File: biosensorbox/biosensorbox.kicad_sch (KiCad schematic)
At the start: 42 parts, among them J1 USB_B_Mini, J2 ECG1, J3 ECG2, Q1 NMOS, SW1 BootButton, SW2 ResetButton, U1 ESP32-S3-WROOM-1, U2 TPD2EUSB30, U3 BMI270, U4 OPA325, U5 PUS-0503.3-2W

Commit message: Updated DC/DC Converter Capacitor values
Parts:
- C11: value 10u -> 0.47u
- C12: value 10u -> 33u
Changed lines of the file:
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@@
       (effects (font (size 1.27 1.27)) (justify left))
     )
-    (property "Value" "10u" (at 237.49 85.09 0)
+    (property "Value" "33u" (at 237.49 85.09 0)
       (effects (font (size 1.27 1.27)) (justify left))
     )
@@
       (effects (font (size 1.27 1.27)) (justify left))
     )
-    (property "Value" "10u" (at 273.05 85.09 0)
-      (effects (font (size 1.27 1.27)) (justify left))
-    )
+    (property "Value" "0.47u" (at 273.05 85.09 0)
+      (effects (font (size 1.27 1.27)) (justify left))
+    )

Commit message: Latest updates to the schematic
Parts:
- removed J2: ECG1, symbol Connector_Generic:Conn_01x01
- removed J3: ECG2, symbol Connector_Generic:Conn_01x01
- added J4: Display, symbol Connector_Generic:Conn_01x05
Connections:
- net GND: now also Q1.3 (S); no longer Q1.1 (D)
- net at R4.1, R5.1, R6.1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: now also Q1.1 (D); no longer Q1.3 (S)
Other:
- note removed: "TODO : ECG Electrodes + Instrumenting amplifier"
- moved on the sheet: Q1
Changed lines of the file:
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@@
-    (effects (font (size 1.27 1.27)) (justify left bottom))
-  )
-  (text "TODO : ECG Electrodes + Instrumenting amplifier" (at 106.68 151.13 0)
     (effects (font (size 1.27 1.27)) (justify left bottom))
   )
@@
     )
   )
-  (symbol (lib_id "Connector_Generic:Conn_01x01") (at 113.03 140.97 180) (unit 1)
-    (in_bom yes) (on_board yes) (dnp no) (fields_autoplaced)
-    (property "Reference" "J3" (at 113.03 134.62 0)
-      (effects (font (size 1.27 1.27)))
-    )
-    (property "Value" "ECG2" (at 113.03 137.16 0)
-      (effects (font (size 1.27 1.27)))
-    )
-    (property "Footprint" "" (at 113.03 140.97 0)
-      (effects (font (size 1.27 1.27)) hide)
-    )
-    (property "Datasheet" "~" (at 113.03 140.97 0)
-      (effects (font (size 1.27 1.27)) hide)
-    )
-    (pin "1")
-    (instances
-      (project "biosensorbox"
-        (path "/b5418477-9d8b-43d2-97f7-47051a4a367a"
-          (reference "J3") (unit 1)
-        )
-      )
-    )
-  )
   (symbol (lib_id "Device:R") (at 45.72 182.88 270) (mirror x) (unit 1)
     (in_bom yes) (on_board yes) (dnp no) (fields_autoplaced)
@@
         (path "/b5418477-9d8b-43d2-97f7-47051a4a367a"
           (reference "C10") (unit 1)
+        )
+      )
+    )
+  )
+  (symbol (lib_id "Connector_Generic:Conn_01x05") (at 185.42 140.97 270) (unit 1)
+    (in_bom yes) (on_board yes) (dnp no) (fields_autoplaced)
+    (property "Reference" "J4" (at 185.42 144.78 90)
+      (effects (font (size 1.27 1.27)))
+    )
+    (property "Value" "Display" (at 185.42 147.32 90)
+      (effects (font (size 1.27 1.27)))
+    )
+    (property "Footprint" "" (at 185.42 140.97 0)
+      (effects (font (size 1.27 1.27)) hide)
+    )
+    (property "Datasheet" "~" (at 185.42 140.97 0)
+      (effects (font (size 1.27 1.27)) hide)
+    )
+    (pin "2")
+    (pin "1")
+    (pin "3")
+    (pin "4")
+    (pin "5")
+    (instances
+      (project "biosensorbox"
+        (path "/b5418477-9d8b-43d2-97f7-47051a4a367a"
+          (reference "J4") (unit 1)
         )
       )
@@
     )
   )
-  (symbol (lib_id "Connector_Generic:Conn_01x01") (at 137.16 140.97 0) (unit 1)
-    (in_bom yes) (on_board yes) (dnp no)
-    (property "Reference" "J2" (at 135.89 134.62 0)
-      (effects (font (size 1.27 1.27)) (justify left))
-    )
-    (property "Value" "ECG1" (at 134.62 137.16 0)
-      (effects (font (size 1.27 1.27)) (justify left))
-    )
-    (property "Footprint" "" (at 137.16 140.97 0)
-      (effects (font (size 1.27 1.27)) hide)
-    )
-    (property "Datasheet" "~" (at 137.16 140.97 0)
-      (effects (font (size 1.27 1.27)) hide)
-    )
-    (pin "1")
-    (instances
-      (project "biosensorbox"
-        (path "/b5418477-9d8b-43d2-97f7-47051a4a367a"
-          (reference "J2") (unit 1)
-        )
-      )
-    )
-  )
   (symbol (lib_id "Device:Fuse") (at 274.32 78.74 90) (unit 1)
     (in_bom yes) (on_board yes) (dnp no) (fields_autoplaced)
@@
     )
   )
-  (symbol (lib_id "Simulation_SPICE:NMOS") (at 63.5 180.34 270) (unit 1)
-    (in_bom yes) (on_board yes) (dnp no) (fields_autoplaced)
+  (symbol (lib_id "Simulation_SPICE:NMOS") (at 63.5 180.34 90) (mirror x) (unit 1)
+    (in_bom yes) (on_board yes) (dnp no)
     (property "Reference" "Q1" (at 63.5 186.69 90)
       (effects (font (size 1.27 1.27)))
@@
       (effects (font (size 1.27 1.27)))
     )
-    (property "Footprint" "" (at 66.04 185.42 0)
-      (effects (font (size 1.27 1.27)) hide)
-    )
-    (property "Datasheet" "https://ngspice.sourceforge.io/docs/ngspice-manual.pdf" (at 50.8 180.34 0)
-      (effects (font (size 1.27 1.27)) hide)
-    )
-    (property "Sim.Device" "NMOS" (at 46.355 180.34 0)
-      (effects (font (size 1.27 1.27)) hide)
-    )
-    (property "Sim.Type" "VDMOS" (at 44.45 180.34 0)
-      (effects (font (size 1.27 1.27)) hide)
-    )
-    (property "Sim.Pins" "1=D 2=G 3=S" (at 48.26 180.34 0)
-      (effects (font (size 1.27 1.27)) hide)
-    )
+    (property "Footprint" "" (at 60.96 185.42 0)
+      (effects (font (size 1.27 1.27)) hide)
+    )
+    (property "Datasheet" "https://ngspice.sourceforge.io/docs/ngspice-manual.pdf" (at 76.2 180.34 0)
+      (effects (font (size 1.27 1.27)) hide)
+    )
+    (property "Sim.Device" "NMOS" (at 80.645 180.34 0)
+      (effects (font (size 1.27 1.27)) hide)
+    )
+    (property "Sim.Type" "VDMOS" (at 82.55 180.34 0)
+      (effects (font (size 1.27 1.27)) hide)
+    )
+    (property "Sim.Pins" "1=D 2=G 3=S" (at 78.74 180.34 0)
+      (effects (font (size 1.27 1.27)) hide)
+    )

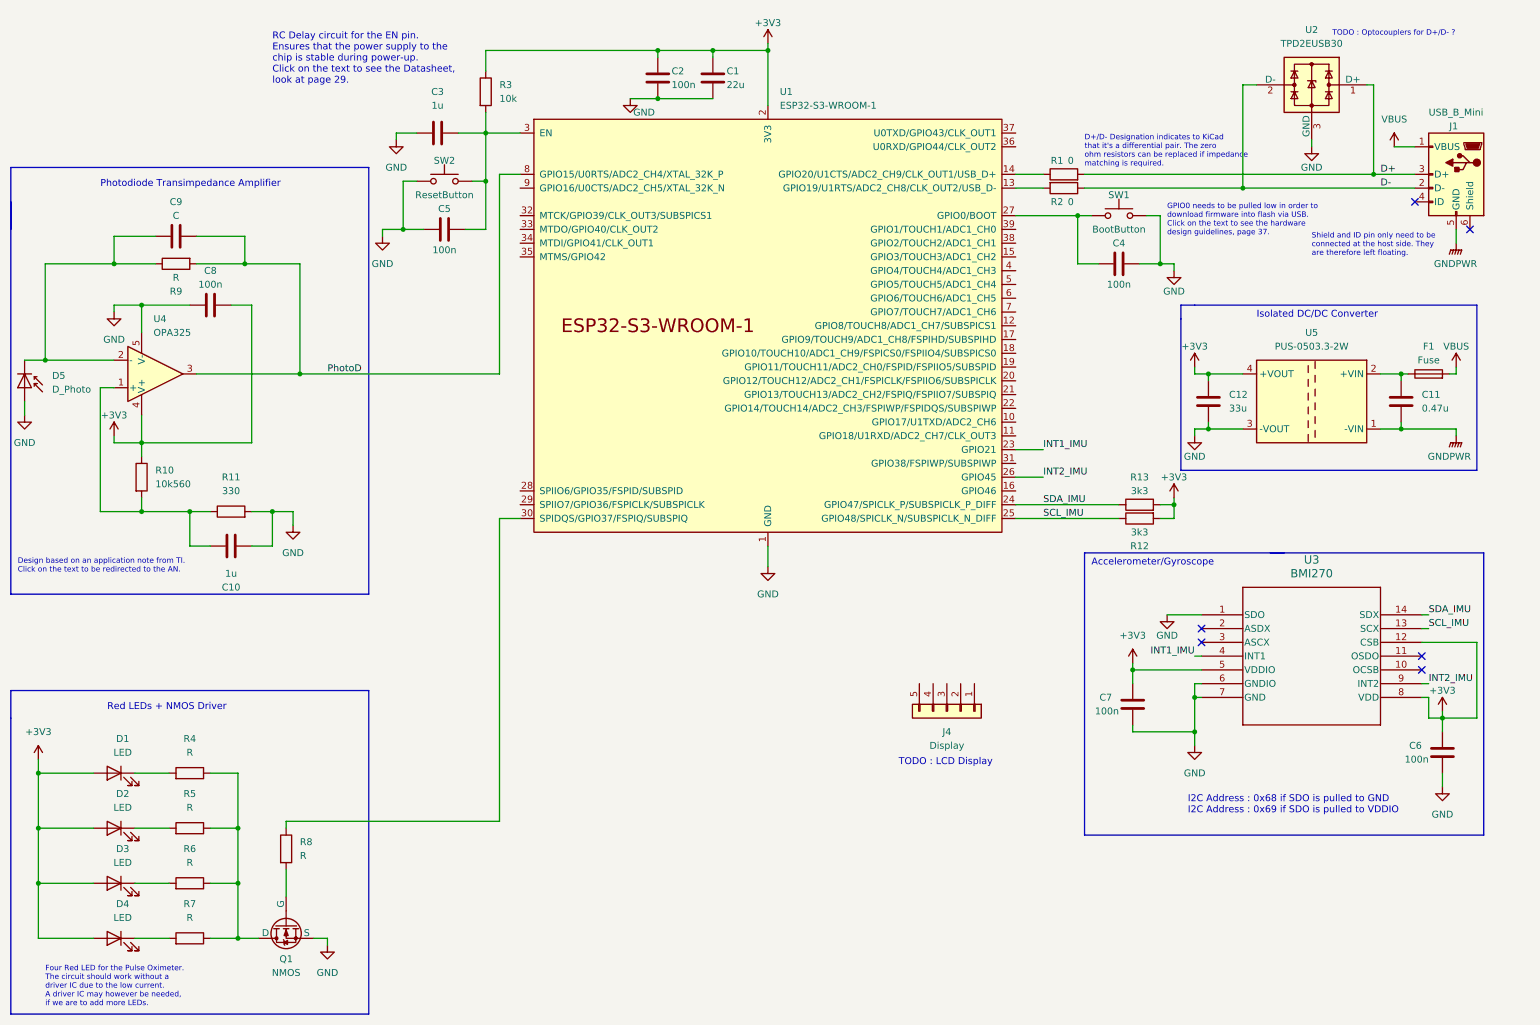
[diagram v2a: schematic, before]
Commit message: Finished Schematic and started Layout
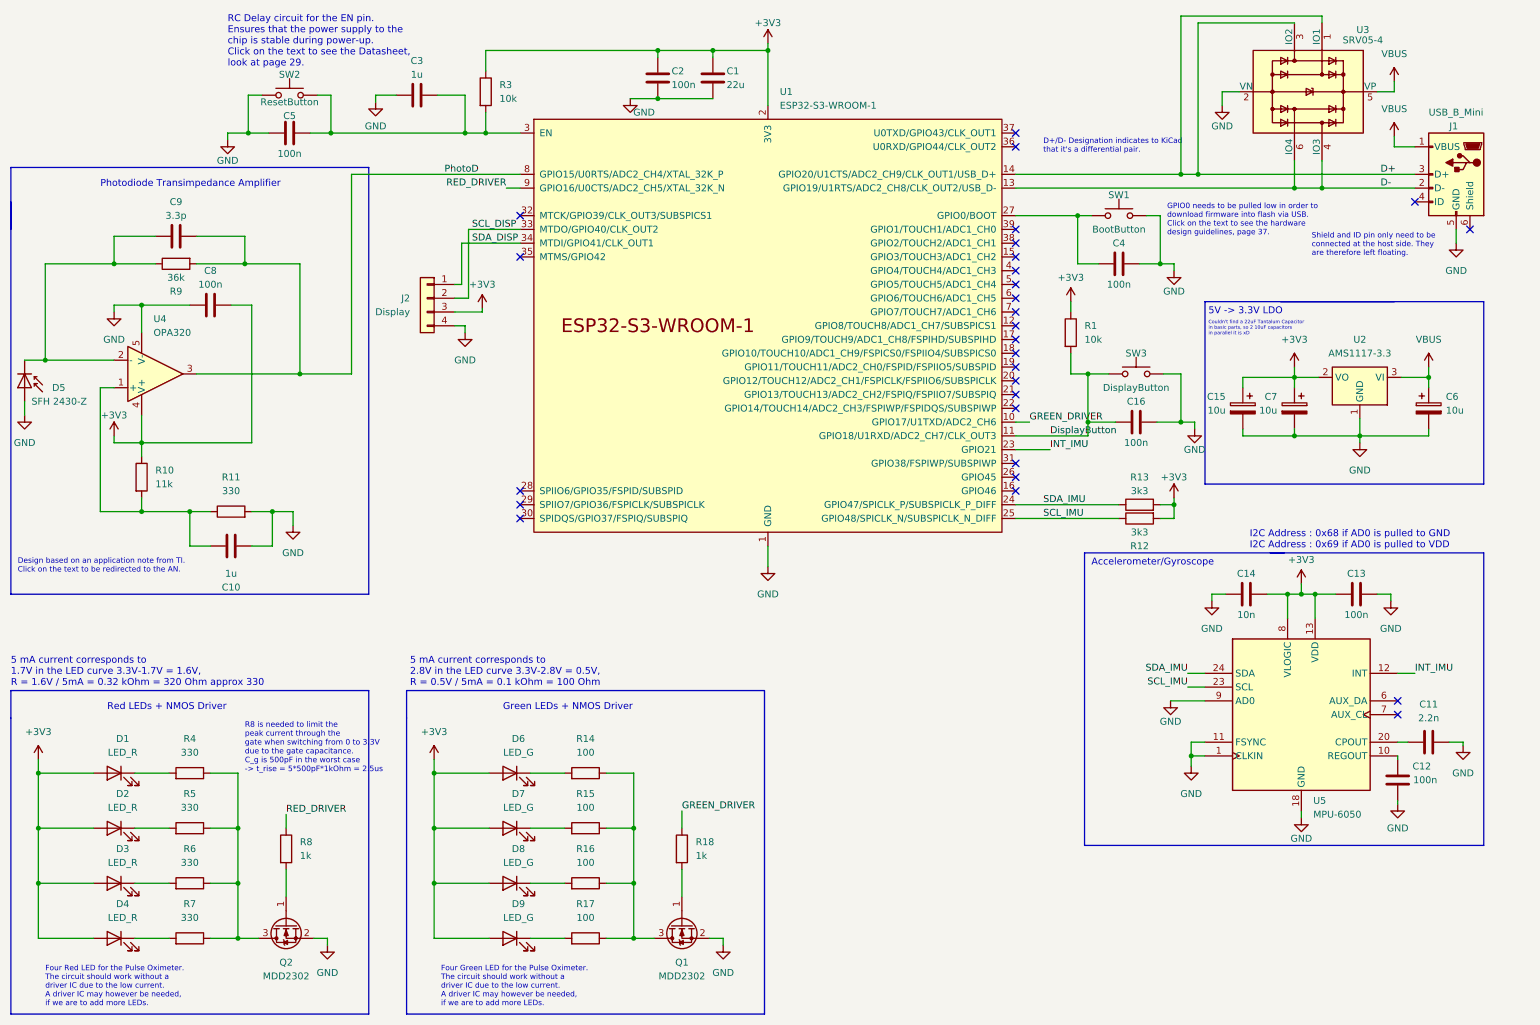
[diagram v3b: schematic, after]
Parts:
- removed C6, C7: 100n, symbol Device:C
- removed F1: Fuse, symbol Device:Fuse
- removed J4: Display, symbol Connector_Generic:Conn_01x05
- removed Q1: NMOS, symbol Simulation_SPICE:NMOS
- removed R2: 0, symbol Device:R
- removed U2: TPD2EUSB30, Package_TO_SOT_SMD:Texas_DRT-3, symbol Power_Protection:TPD2EUSB30
- removed U3: BMI270, symbol UL_Bosch_IMU:BMI270
- removed U5: PUS-0503.3-2W, symbol Regulator_Switching:CRE1S0505S3C
- added C13, C16: 100n, Capacitor_SMD:C_0603_1608Metric, symbol Device:C
- added C14: 10n, Capacitor_SMD:C_0603_1608Metric, symbol Device:C
- added C15, C6, C7: 10u, Capacitor_Tantalum_SMD:CP_EIA-3216-18_Kemet-A, symbol Device:C_Polarized
- added D6, D7, D8, D9: LED_G, LED_SMD:LED_0603_1608Metric, symbol Device:LED
- added J2: Display, Connector_PinHeader_2.54mm:PinHeader_1x04_P2.54mm_Vertical, symbol Connector_Generic:Conn_01x04
- added Q1, Q2: MDD2302, Package_TO_SOT_SMD:SOT-23, symbol Device:Q_NMOS_GSD
- added R14, R15, R16, R17: 100, Resistor_SMD:R_0603_1608Metric, symbol Device:R
- added R18: 1k, Resistor_SMD:R_0603_1608Metric, symbol Device:R
- added SW3: DisplayButton, Button_Switch_SMD:SW_Push_1P1T_XKB_TS-1187A, symbol Switch:SW_Push
- added U2: AMS1117-3.3, Package_TO_SOT_SMD:SOT-223-3_TabPin2, symbol Regulator_Linear:AMS1117-3.3
- added U3: SRV05-4, Package_TO_SOT_SMD:SOT-23-6, symbol Power_Protection:SRV05-4
- added U5: MPU-6050, Sensor_Motion:InvenSense_QFN-24_4x4mm_P0.5mm, symbol Sensor_Motion:MPU-6050
- C1: footprint (none) -> Capacitor_SMD:C_1206_3216Metric
- C10, C3: footprint (none) -> Capacitor_SMD:C_0805_2012Metric
- C11: value 0.47u -> 2.2n; footprint (none) -> Capacitor_SMD:C_0603_1608Metric
- C12: value 33u -> 100n; footprint (none) -> Capacitor_SMD:C_0603_1608Metric
- C2, C4, C5, C8: footprint (none) -> Capacitor_SMD:C_0603_1608Metric
- C9: value C -> 3.3p; footprint (none) -> Capacitor_SMD:C_0402_1005Metric
- D1, D2, D3, D4: value LED -> LED_R; footprint (none) -> LED_SMD:LED_0603_1608Metric
- D5: value D_Photo -> SFH 2430-Z; footprint (none) -> OptoDevice:Osram_SFH2430
- J1: footprint (none) -> Connector_USB:USB_Mini-B_Wuerth_65100516121_Horizontal
- R1: value 0 -> 10k; footprint (none) -> Resistor_SMD:R_0603_1608Metric
- R10: value 10k560 -> 11k; footprint (none) -> Resistor_SMD:R_0805_2012Metric
- R11, R12, R13, R3: footprint (none) -> Resistor_SMD:R_0603_1608Metric
- R4, R5, R6, R7: value R -> 330; footprint (none) -> Resistor_SMD:R_0603_1608Metric
- R8: value R -> 1k; footprint (none) -> Resistor_SMD:R_0603_1608Metric
- R9: value R -> 36k; footprint (none) -> Resistor_SMD:R_0805_2012Metric
- SW1, SW2: footprint (none) -> Button_Switch_SMD:SW_Push_1P1T_XKB_TS-1187A
- U4: value OPA325 -> OPA320; footprint (none) -> Package_TO_SOT_SMD:SOT-23-5
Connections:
- net GNDPWR is gone; now on net GND: C11.2, J1.5 (GND)
- net +3V3: now also R1.1, C13.1, C14.1, C15.1, C7.1, D6.2 (A), D7.2 (A), D8.2 (A), D9.2 (A), J2.3 (Pin_3), U2.2 (VO), U5.13 (VDD), U5.8 (VLOGIC); no longer C12.1
- net D+: now also U1.14 (GPIO20/U1CTS/ADC2_CH9/CLK_OUT1/USB_D+), U3.1 (IO1), U3.3 (IO2); no longer R1.2
- net D-: now also U1.13 (GPIO19/U1RTS/ADC2_CH8/CLK_OUT2/USB_D-), U3.4 (IO3), U3.6 (IO4)
- net GND: now also C13.2, C14.2, C15.2, C16.1, C6.2, C7.2, J2.4 (Pin_4), Q1.2 (S), Q2.2 (S), SW3.1, U2.1 (GND), U3.2 (VN), U5.1 (CLKIN), U5.11 (FSYNC), U5.18 (GND), U5.9 (AD0)
- net SCL_IMU: now also U5.23 (SCL)
- net SDA_IMU: now also U5.24 (SDA)
- net VBUS: now also C6.1, U2.3 (VI), U3.5 (VP)
- net at R4.1, R5.1, R6.1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: now also Q2.3 (D)
- net GREEN_DRIVER: now reaches U1.10 (GPIO17/U1TXD/ADC2_CH6)
- net GREEN_DRIVER: now also R18.1
- net DisplayButton: now reaches U1.11 (GPIO18/U1RXD/ADC2_CH7/CLK_OUT3)
- net DisplayButton: now also R1.2, C16.2, SW3.2
- net at U1.30 (SPIDQS/GPIO37/FSPIQ/SUBSPIQ): no longer R8.1
- net SCL_DISP: now reaches U1.33 (MTDO/GPIO40/CLK_OUT2)
- net SCL_DISP: now also J2.2 (Pin_2)
- net SDA_DISP: now reaches U1.34 (MTDI/GPIO41/CLK_OUT1)
- net SDA_DISP: now also J2.1 (Pin_1)
- net RED_DRIVER: now reaches U1.9 (GPIO16/U0CTS/ADC2_CH5/XTAL_32K_N)
- net RED_DRIVER: now also R8.1
- net at R8.2: now also Q2.1 (G)
- net at C11.1: now also U5.20 (CPOUT)
- net INT1_IMU renamed INT_IMU
- net INT_IMU: now also U5.12 (INT)
- net INT2_IMU: no longer names the net of U1.26 (GPIO45)
- new net: D6.1 (K), R14.2
- new net: D9.1 (K), R17.2
- new net: C12.1, U5.10 (REGOUT)
- new net: Q1.1 (G), R18.2
- new net: Q1.3 (D), R14.1, R15.1, R16.1, R17.1
- new net: D8.1 (K), R16.2
- new net: D7.1 (K), R15.2
- no-connect marks 6 -> 28
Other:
- note added: "5 mA current corresponds to 1.7V in the LED curve 3.3V-1.7V = 1.6V, R = 1.6V / 5mA = 0.32 kOhm = 320 Ohm approx 330"
- note added: "5 mA current corresponds to 2.8V in the LED curve 3.3V-2.8V = 0.5V, R = 0.5V / 5mA = 0.1 kOhm = 100 Ohm"
- note added: "5V -> 3.3V LDO"
- note added: "Couldn't find a 22uF Tantalum Capacitor in basic parts, so 2 10uF capacitors in parallel it is xD"
- note added: "D+/D- Designation indicates to KiCad that it's a differential pair."
- note added: "Four Green LED for the Pulse Oximeter. The circuit should work without a driver IC due to the low current. A driver IC may however be needed, if we are to add more LEDs."
- note added: "Green LEDs + NMOS Driver"
- note added: "I2C Address : 0x68 if AD0 is pulled to GND I2C Address : 0x69 if AD0 is pulled to VDD"
- note added: "R8 is needed to limit the peak current through the gate when switching from 0 to 3.3V due to the gate capacitance. C_g is 500pF in the worst case -> t_rise = 5*500pF*1kOhm = 2.5us"
- note removed: "D+/D- Designation indicates to KiCad that it's a differential pair. The zero ohm resistors can be replaced if impedance matching is required."
- note removed: "I2C Address : 0x68 if SDO is pulled to GND I2C Address : 0x69 if SDO is pulled to VDDIO"
- note removed: "Isolated DC/DC Converter"
- note removed: "TODO : LCD Display"
- note removed: "TODO : Optocouplers for D+/D- ?"
- moved on the sheet: C3, C5, SW2
